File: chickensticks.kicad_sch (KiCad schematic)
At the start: 4 parts

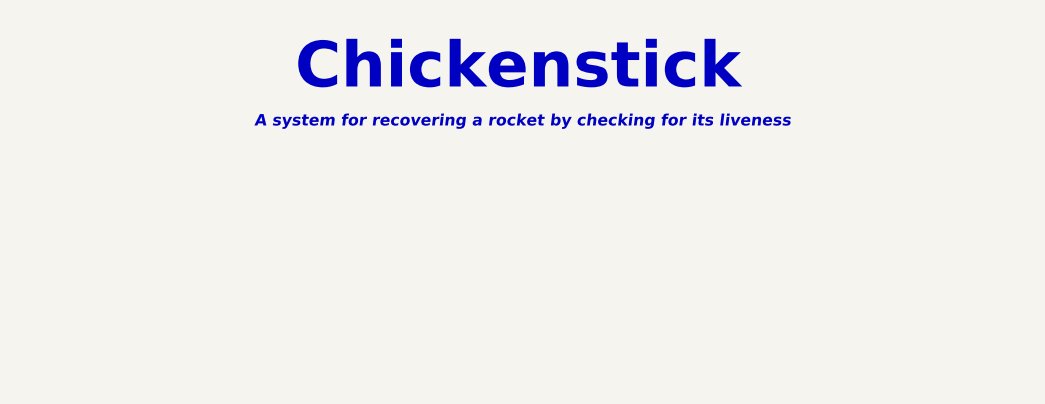
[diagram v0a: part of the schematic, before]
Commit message: Remove big SS14 diodes
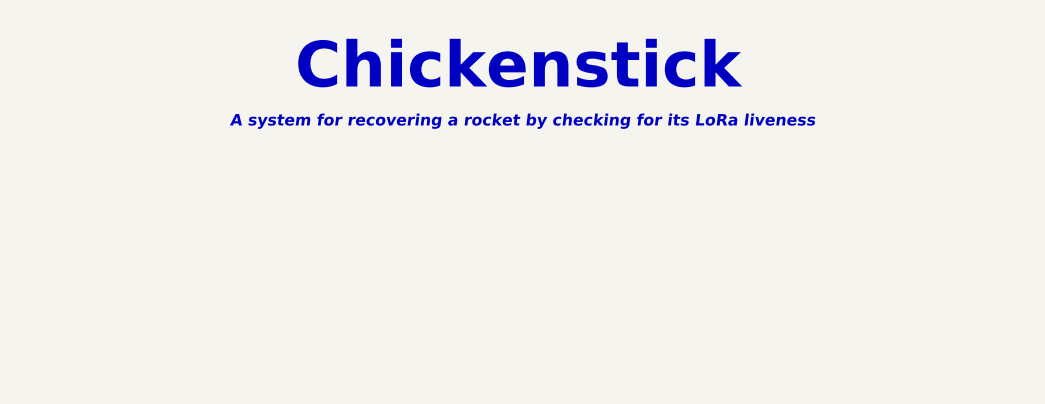
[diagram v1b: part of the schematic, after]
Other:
- note added: "A system for recovering a rocket by checking for its LoRa liveness"
- note removed: "A system for recovering a rocket by checking for its liveness"
